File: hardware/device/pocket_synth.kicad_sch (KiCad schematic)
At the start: 0 parts

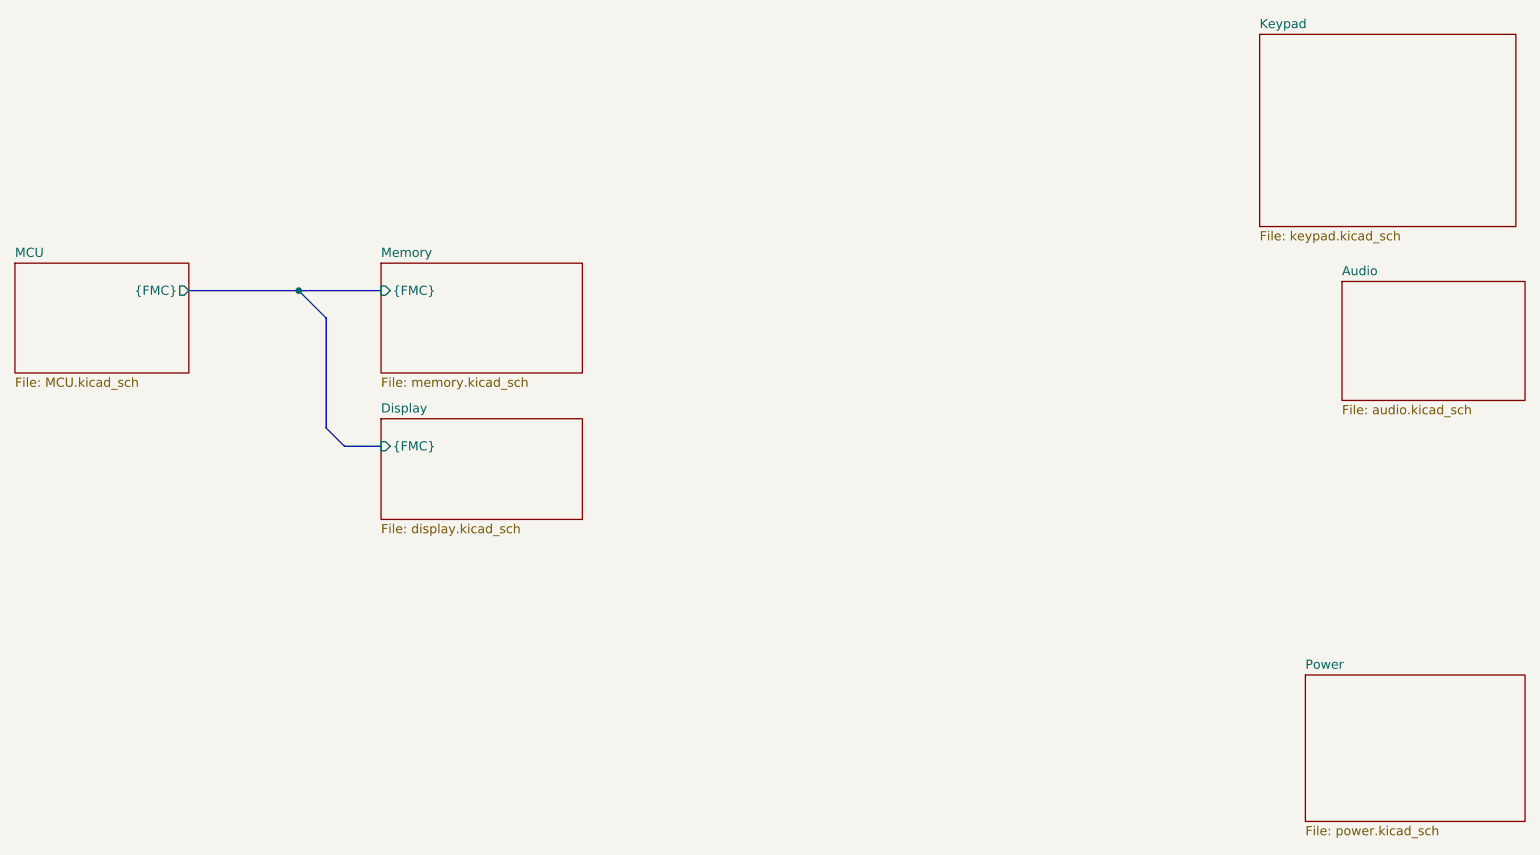
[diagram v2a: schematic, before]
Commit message: feat: start codec layout
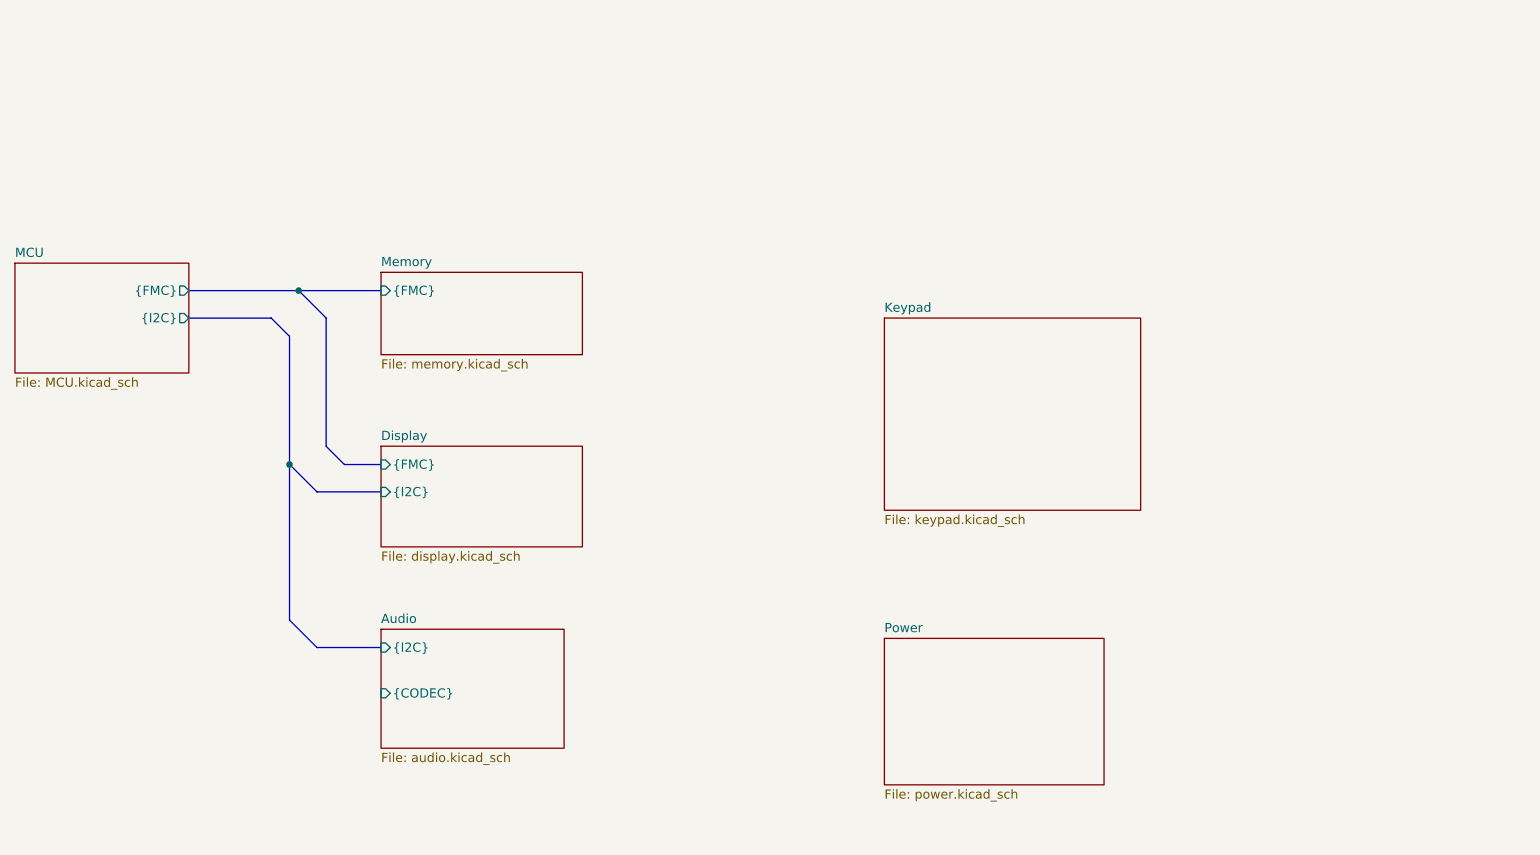
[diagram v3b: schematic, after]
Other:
- sheet Audio ports: added {CODEC}, {I2C}; removed none
- sheet Display ports: added {I2C}; removed none
- sheet MCU ports: added {I2C}; removed none
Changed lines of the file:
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@@
+	)
+	(junction
+		(at 101.6 78.74)
+		(diameter 0)
+		(color 0 0 0 0)
 	)
 	(junction
@@
 	(bus
 		(pts
-			(xy 106.68 58.42) (xy 106.68 73.66)
-		)
-		(stroke
-			(width 0)
-			(type default)
-		)
-	)
-	(bus
-		(pts
-			(xy 109.22 76.2) (xy 114.3 76.2)
-		)
-		(stroke
-			(width 0)
-			(type default)
-		)
-	)
-	(bus
-		(pts
-			(xy 106.68 73.66) (xy 109.22 76.2)
+			(xy 106.68 58.42) (xy 106.68 76.2)
+		)
+		(stroke
+			(width 0)
+			(type default)
+		)
+	)
+	(bus
+		(pts
+			(xy 105.41 104.14) (xy 114.3 104.14)
+		)
+		(stroke
+			(width 0)
+			(type default)
+		)
+	)
+	(bus
+		(pts
+			(xy 101.6 78.74) (xy 101.6 100.33)
+		)
+		(stroke
+			(width 0)
+			(type default)
+		)
+	)
+	(bus
+		(pts
+			(xy 109.22 78.74) (xy 114.3 78.74)
+		)
+		(stroke
+			(width 0)
+			(type default)
+		)
+	)
+	(bus
+		(pts
+			(xy 101.6 100.33) (xy 105.41 104.14)
+		)
+		(stroke
+			(width 0)
+			(type default)
+		)
+	)
+	(bus
+		(pts
+			(xy 105.41 82.55) (xy 114.3 82.55)
+		)
+		(stroke
+			(width 0)
+			(type default)
+		)
+	)
+	(bus
+		(pts
+			(xy 99.06 58.42) (xy 101.6 60.96)
+		)
+		(stroke
+			(width 0)
+			(type default)
+		)
+	)
+	(bus
+		(pts
+			(xy 87.63 58.42) (xy 99.06 58.42)
+		)
+		(stroke
+			(width 0)
+			(type default)
+		)
+	)
+	(bus
+		(pts
+			(xy 106.68 76.2) (xy 109.22 78.74)
 		)
 		(stroke
@@
 	(bus
 		(pts
+			(xy 101.6 78.74) (xy 105.41 82.55)
+		)
+		(stroke
+			(width 0)
+			(type default)
+		)
+	)
+	(bus
+		(pts
 			(xy 87.63 54.61) (xy 102.87 54.61)
+		)
+		(stroke
+			(width 0)
+			(type default)
+		)
+	)
+	(bus
+		(pts
+			(xy 101.6 60.96) (xy 101.6 78.74)
 		)
 		(stroke
@@
 		(pin "{FMC}" output
 			(at 87.63 54.61 0)
+			(effects
+				(font
+					(size 1.27 1.27)
+				)
+				(justify right)
+			)
+		)
+		(pin "{I2C}" output
+			(at 87.63 58.42 0)
 			(effects
 				(font
@@
 	)
 	(sheet
-		(at 242.57 107.95)
+		(at 184.15 102.87)
 		(size 30.48 20.32)
 		(exclude_from_sim no)
@@
 		)
 		(property "Sheetname" "Power"
-			(at 242.57 107.2384 0)
+			(at 184.15 102.1584 0)
 			(effects
 				(font
@@
 		)
 		(property "Sheetfile" "power.kicad_sch"
-			(at 242.57 128.8546 0)
+			(at 184.15 123.7746 0)
 			(effects
 				(font
@@
 	)
 	(sheet
-		(at 236.22 19.05)
+		(at 184.15 58.42)
 		(size 35.56 26.67)
 		(exclude_from_sim no)
@@
 		)
 		(property "Sheetname" "Keypad"
-			(at 236.22 18.3384 0)
+			(at 184.15 57.7084 0)
 			(effects
 				(font
@@
 		)
 		(property "Sheetfile" "keypad.kicad_sch"
-			(at 236.22 46.3046 0)
+			(at 184.15 85.6746 0)
 			(effects
 				(font
@@
 	)
 	(sheet
-		(at 247.65 53.34)
+		(at 114.3 101.6)
 		(size 25.4 16.51)
 		(exclude_from_sim no)
@@
 		)
 		(property "Sheetname" "Audio"
-			(at 247.65 52.6284 0)
+			(at 114.3 100.8884 0)
 			(effects
 				(font
@@
 		)
 		(property "Sheetfile" "audio.kicad_sch"
-			(at 247.65 70.4346 0)
-			(effects
-				(font
-					(size 1.27 1.27)
-				)
-				(justify left top)
+			(at 114.3 118.6946 0)
+			(effects
+				(font
+					(size 1.27 1.27)
+				)
+				(justify left top)
+			)
+		)
+		(pin "{CODEC}" input
+			(at 114.3 110.49 180)
+			(effects
+				(font
+					(size 1.27 1.27)
+				)
+				(justify left)
+			)
+		)
+		(pin "{I2C}" input
+			(at 114.3 104.14 180)
+			(effects
+				(font
+					(size 1.27 1.27)
+				)
+				(justify left)
 			)
 		)
@@
 	)
 	(sheet
-		(at 114.3 50.8)
-		(size 27.94 15.24)
+		(at 114.3 52.07)
+		(size 27.94 11.43)
 		(exclude_from_sim no)
 		(in_bom yes)
@@
 		)
 		(property "Sheetname" "Memory"
-			(at 114.3 50.0884 0)
+			(at 114.3 51.3584 0)
 			(effects
 				(font
@@
 		)
 		(property "Sheetfile" "memory.kicad_sch"
-			(at 114.3 66.6246 0)
+			(at 114.3 64.0846 0)
 			(effects
 				(font
@@
 	)
 	(sheet
-		(at 114.3 72.39)
+		(at 114.3 76.2)
 		(size 27.94 13.97)
 		(exclude_from_sim no)
@@
 		)
 		(property "Sheetname" "Display"
-			(at 114.3 71.6784 0)
+			(at 114.3 75.4884 0)
 			(effects
 				(font
@@
 		)
 		(property "Sheetfile" "display.kicad_sch"
-			(at 114.3 86.9446 0)
+			(at 114.3 90.7546 0)
 			(effects
 				(font
@@
 		)
 		(pin "{FMC}" input
-			(at 114.3 76.2 180)
-			(effects
-				(font
+			(at 114.3 78.74 180)
+			(effects
+				(font
+					(size 1.27 1.27)
+				)
+				(justify left)
+			)
+		)
+		(pin "{I2C}" input
+			(at 114.3 82.55 180)
+			(effects
+				(font

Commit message: feat: various layouts, changed SDRAM to BGA
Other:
- sheet Keypad ports: added KEYPAD_INT, {I2C}; removed none
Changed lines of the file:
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@@
+	)
+	(junction
+		(at 101.6 100.33)
+		(diameter 0)
+		(color 0 0 0 0)
 	)
 	(junction
@@
 	(bus
 		(pts
-			(xy 105.41 104.14) (xy 114.3 104.14)
+			(xy 105.41 129.54) (xy 114.3 129.54)
+		)
+		(stroke
+			(width 0)
+			(type default)
+		)
+	)
+	(bus
+		(pts
+			(xy 101.6 100.33) (xy 101.6 125.73)
+		)
+		(stroke
+			(width 0)
+			(type default)
+		)
+	)
+	(bus
+		(pts
+			(xy 109.22 78.74) (xy 114.3 78.74)
+		)
+		(stroke
+			(width 0)
+			(type default)
+		)
+	)
+	(bus
+		(pts
+			(xy 105.41 104.14) (xy 101.6 100.33)
+		)
+		(stroke
+			(width 0)
+			(type default)
+		)
+	)
+	(bus
+		(pts
+			(xy 101.6 125.73) (xy 105.41 129.54)
+		)
+		(stroke
+			(width 0)
+			(type default)
+		)
+	)
+	(bus
+		(pts
+			(xy 105.41 82.55) (xy 114.3 82.55)
+		)
+		(stroke
+			(width 0)
+			(type default)
+		)
+	)
+	(bus
+		(pts
+			(xy 99.06 58.42) (xy 101.6 60.96)
+		)
+		(stroke
+			(width 0)
+			(type default)
+		)
+	)
+	(bus
+		(pts
+			(xy 114.3 104.14) (xy 105.41 104.14)
+		)
+		(stroke
+			(width 0)
+			(type default)
+		)
+	)
+	(bus
+		(pts
+			(xy 87.63 58.42) (xy 99.06 58.42)
 		)
 		(stroke
@@
 		(pts
 			(xy 101.6 78.74) (xy 101.6 100.33)
-		)
-		(stroke
-			(width 0)
-			(type default)
-		)
-	)
-	(bus
-		(pts
-			(xy 109.22 78.74) (xy 114.3 78.74)
-		)
-		(stroke
-			(width 0)
-			(type default)
-		)
-	)
-	(bus
-		(pts
-			(xy 101.6 100.33) (xy 105.41 104.14)
-		)
-		(stroke
-			(width 0)
-			(type default)
-		)
-	)
-	(bus
-		(pts
-			(xy 105.41 82.55) (xy 114.3 82.55)
-		)
-		(stroke
-			(width 0)
-			(type default)
-		)
-	)
-	(bus
-		(pts
-			(xy 99.06 58.42) (xy 101.6 60.96)
-		)
-		(stroke
-			(width 0)
-			(type default)
-		)
-	)
-	(bus
-		(pts
-			(xy 87.63 58.42) (xy 99.06 58.42)
 		)
 		(stroke
@@
 	)
 	(sheet
-		(at 184.15 58.42)
-		(size 35.56 26.67)
+		(at 114.3 101.6)
+		(size 25.4 15.24)
 		(exclude_from_sim no)
 		(in_bom yes)
@@
 		)
 		(property "Sheetname" "Keypad"
-			(at 184.15 57.7084 0)
+			(at 114.3 100.8884 0)
 			(effects
 				(font
@@
 		)
 		(property "Sheetfile" "keypad.kicad_sch"
-			(at 184.15 85.6746 0)
+			(at 114.3 117.4246 0)
 			(effects
 				(font
@@
 				)
 				(justify left top)
+			)
+		)
+		(pin "KEYPAD_INT" input
+			(at 114.3 107.95 180)
+			(effects
+				(font
+					(size 1.27 1.27)
+				)
+				(justify left)
+			)
+		)
+		(pin "{I2C}" input
+			(at 114.3 104.14 180)
+			(effects
+				(font
+					(size 1.27 1.27)
+				)
+				(justify left)
 			)
 		)
@@
 	)
 	(sheet
-		(at 114.3 101.6)
+		(at 114.3 127)
 		(size 25.4 16.51)
 		(exclude_from_sim no)
@@
 		)
 		(property "Sheetname" "Audio"
-			(at 114.3 100.8884 0)
+			(at 114.3 126.2884 0)
 			(effects
 				(font
@@
 		)
 		(property "Sheetfile" "audio.kicad_sch"
-			(at 114.3 118.6946 0)
+			(at 114.3 144.0946 0)
 			(effects
 				(font
@@
 		)
 		(pin "{CODEC}" input
-			(at 114.3 110.49 180)
+			(at 114.3 135.89 180)
 			(effects
 				(font
@@
 		)
 		(pin "{I2C}" input
-			(at 114.3 104.14 180)
+			(at 114.3 129.54 180)
 			(effects
 				(font
@@
 	(sheet
 		(at 114.3 52.07)
-		(size 27.94 11.43)
+		(size 25.4 13.97)
 		(exclude_from_sim no)
 		(in_bom yes)
@@
 		)
 		(property "Sheetfile" "memory.kicad_sch"
-			(at 114.3 64.0846 0)
+			(at 114.3 66.6246 0)
 			(effects
 				(font
@@
 	(sheet
 		(at 114.3 76.2)
-		(size 27.94 13.97)
-		(exclude_from_sim no)
-		(in_bom yes)
+		(size 25.4 13.97)
+		(exclude_from_sim no)
+		(in_bom yes)

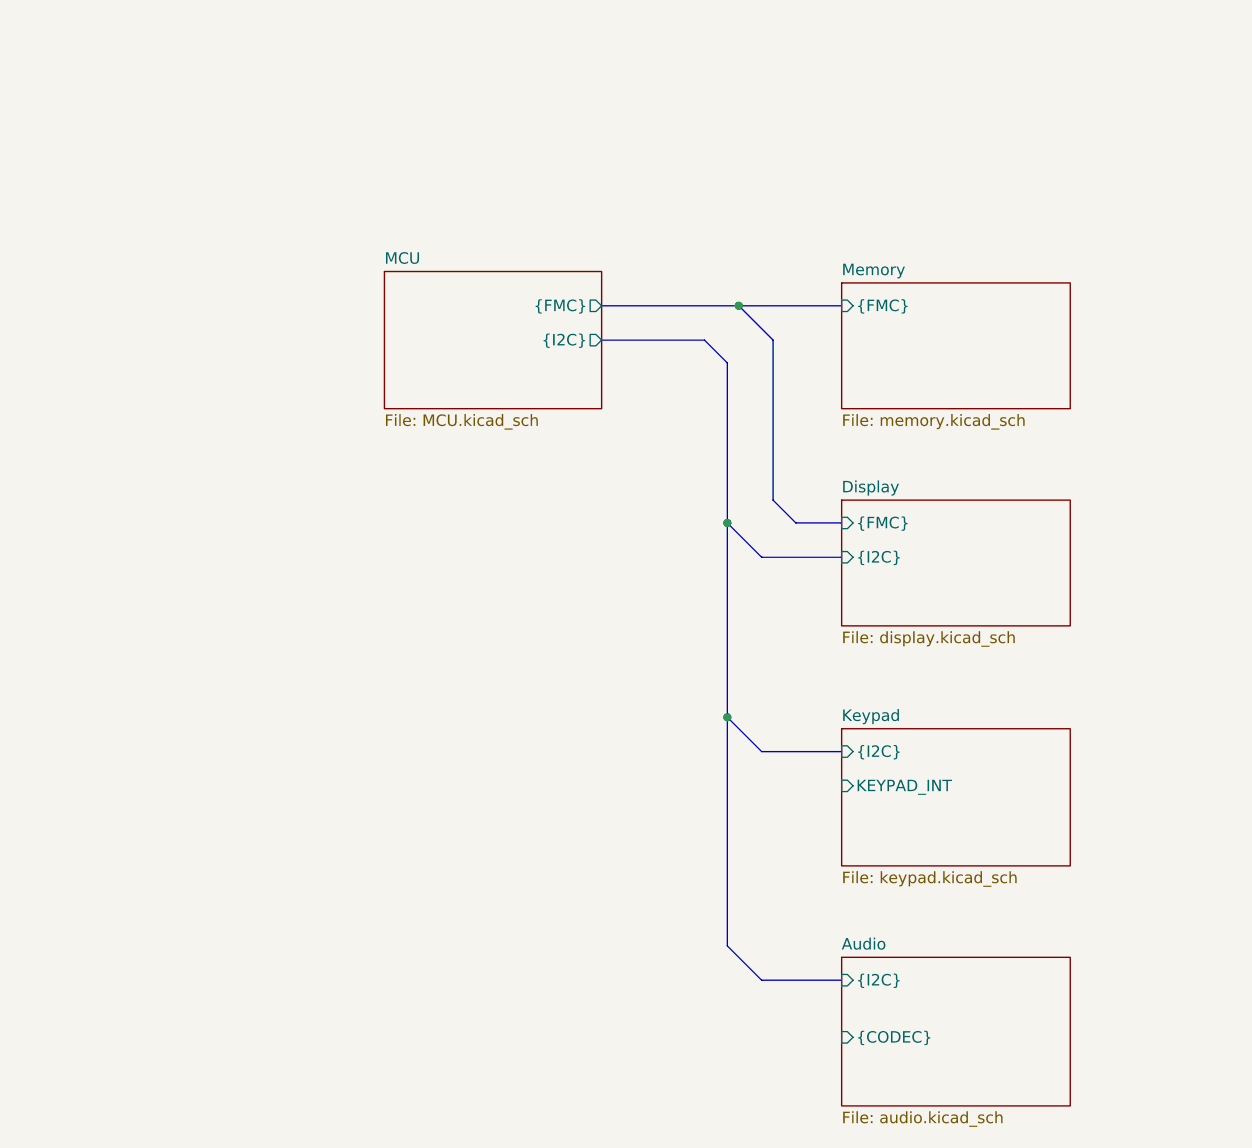
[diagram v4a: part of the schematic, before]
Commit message: feat: BGA routing for SDRAM
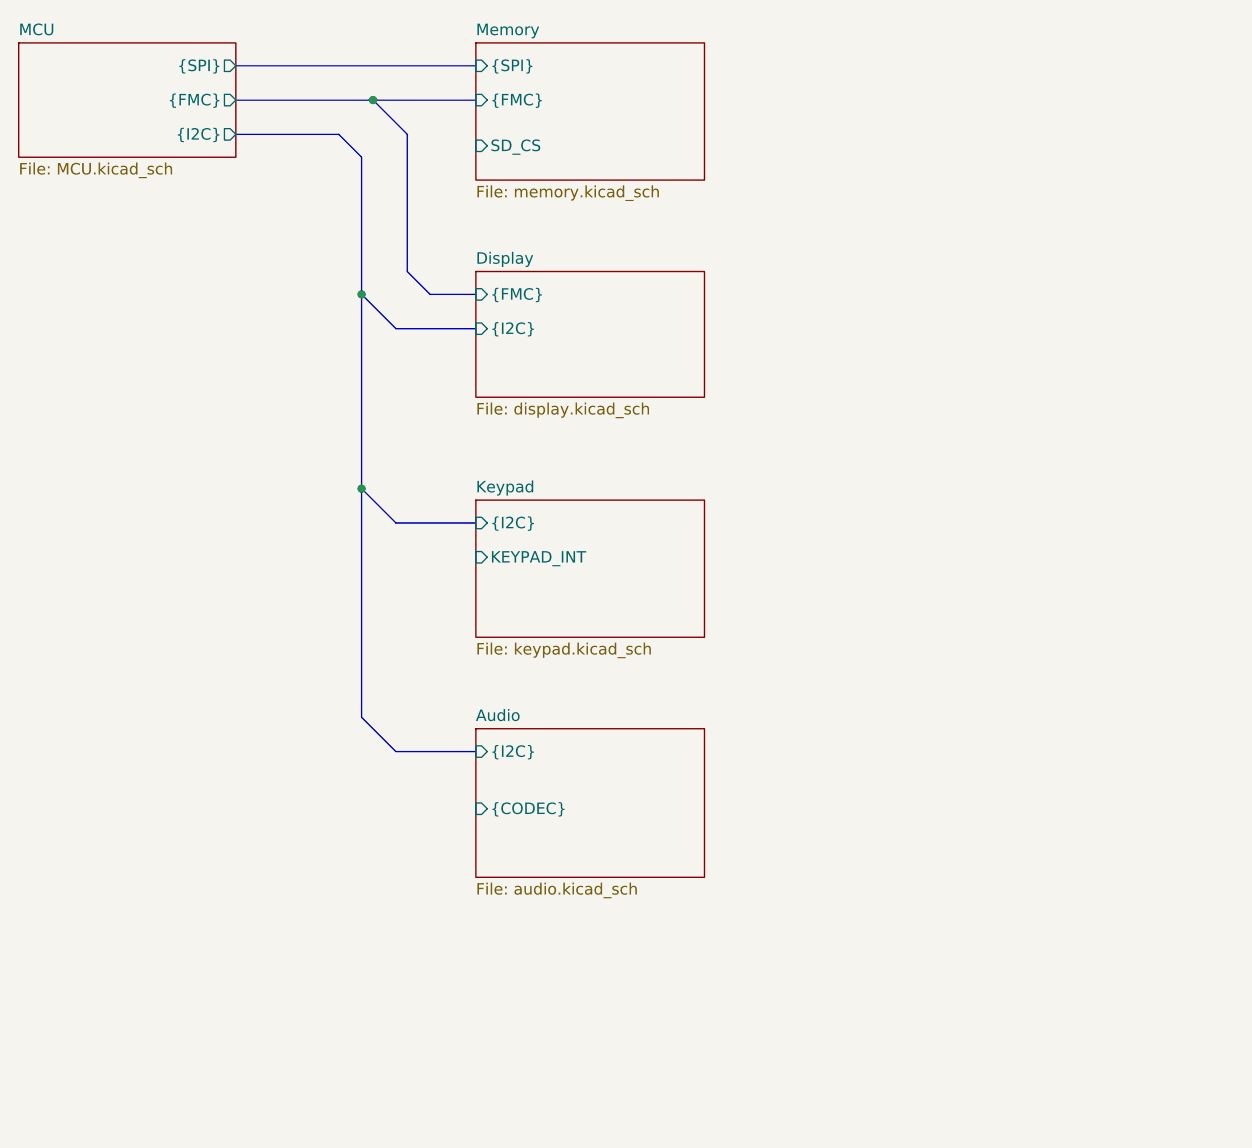
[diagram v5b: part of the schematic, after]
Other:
- sheet MCU ports: added {SPI}; removed none
- sheet Memory ports: added SD_CS, {SPI}; removed none

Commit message: feat: various audio and power schematic layout
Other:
- sheet Audio ports: added CODEC_IRQ; removed none
- sheet Display ports: added DISPLAY_TE; removed none
- sheet MCU ports: added CODEC_IRQ, PWR_SW, USB_D+, USB_D-, {CODEC}, ~{MCU_PWR_EN}; removed none
- sheet Power ports: added 3v3_PG, MCU_PWR_SW, USB_D+, USB_D-, ~{MCU_PWR_EN}; removed none
